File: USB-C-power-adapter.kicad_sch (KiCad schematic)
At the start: 65 parts, among them J1 USB-C_GCT_USB4105-GF-A, J2 JST_SH_1x4_SM04B-SRSS-TB-LF-SN, J3 Conn_Molex_NanoFit_1053131202, Q1 SQS401EN-T1_BE3, U1 TPD4E02B04DQA, U2 SIC477ED-T1-GE3, U3 STUSB4500_QFN, U4 TPD4E02B04DQA

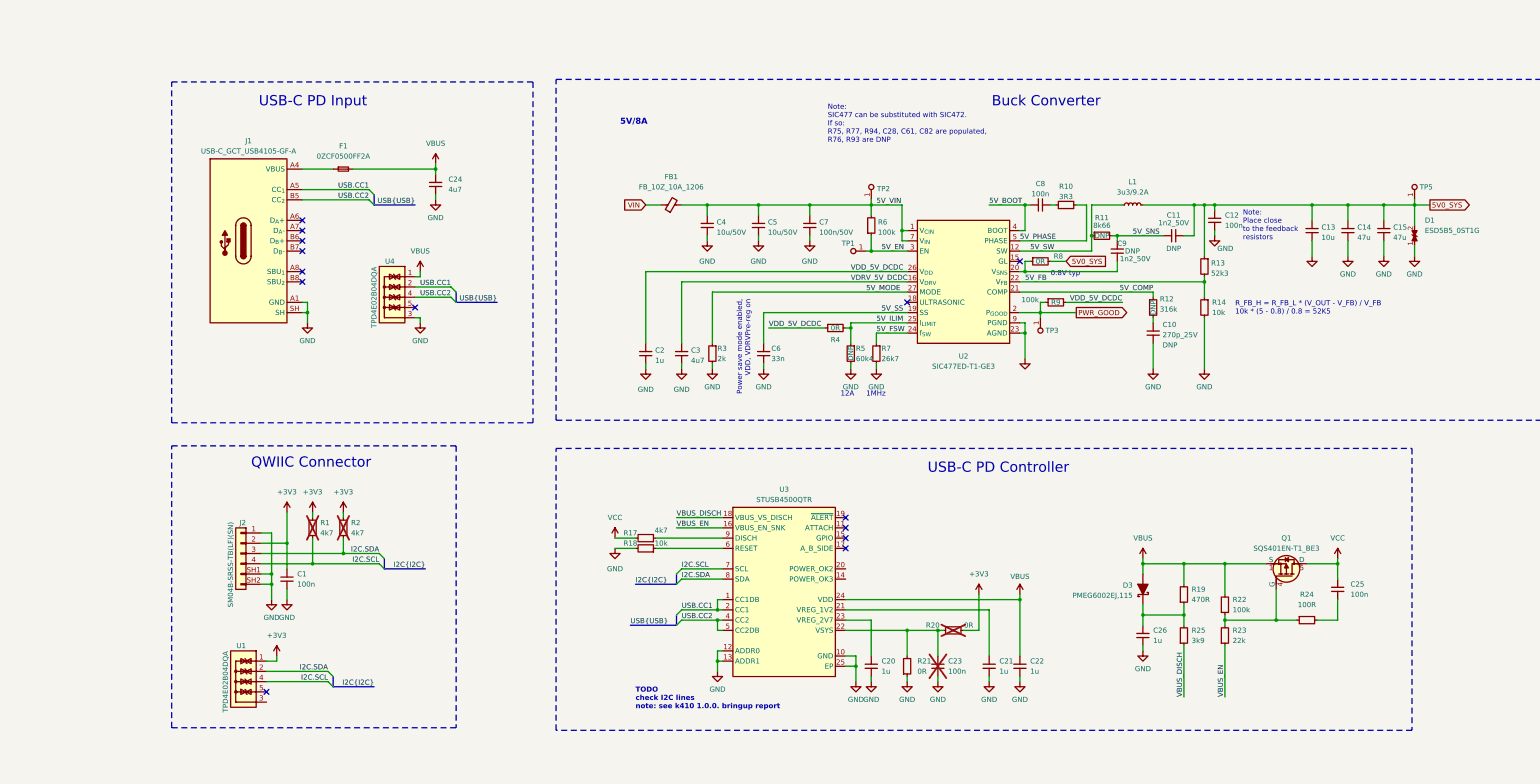
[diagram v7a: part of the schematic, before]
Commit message: [#57006] Change feedback resistors
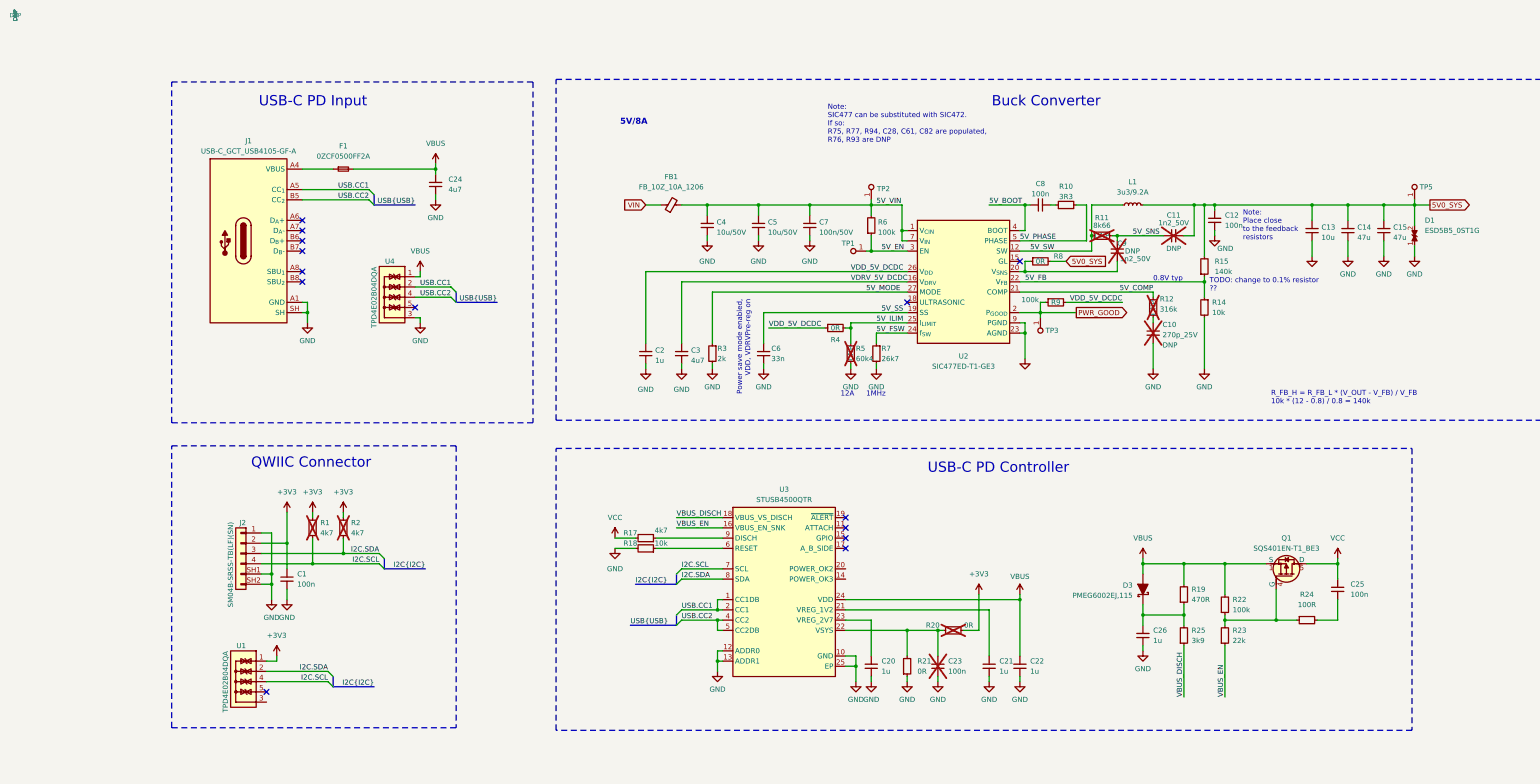
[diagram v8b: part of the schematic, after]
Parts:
- removed R13: R_52k3_0402, antmicro-footprints:R_0402_1005Metric, symbol antmicroResistors0402:R_52k3_0402
- added R15: R_140k_0402, antmicro-footprints:R_0402_1005Metric, symbol antmicroResistors0402:R_140k_0402
- C10, C11, C9, R11, R12, R5: now not fitted; now left out of the parts list
- C23, R1, R2, R20: DNP (none) -> DNP; now left out of the parts list
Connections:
- net 5V0_SYS: now also R15.2
- net 5V_FB: now also R15.1
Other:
- note added: "R_FB_H = R_FB_L * (V_OUT - V_FB) / V_FB 10k * (12 - 0.8) / 0.8 = 140k"
- note added: "TODO: change to 0.1% resistor ??"
- note removed: "R_FB_H = R_FB_L * (V_OUT - V_FB) / V_FB 10k * (5 - 0.8) / 0.8 = 52K5"
- note removed: "TODO check I2C lines note: see k410 1.0.0. bringup report"
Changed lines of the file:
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@@
     (effects (font (size 2.54 2.54)) (justify left bottom))
   )
-  (text "0.8V typ" (at 256.54 64.77 0)
+  (text "0.8V typ" (at 281.94 66.04 0)
     (effects (font (size 1.27 1.27)) (justify left bottom))
   )
@@
   (text "TODO\nadd the MOLEX nano fit 1053131202\nto the library "
     (at 91.44 217.805 0)
-    (effects (font (size 1.27 1.27)) (justify left bottom))
+    (effects (font (size 1.27 1.27) (color 255 0 0 1)) (justify left bottom))
   )
   (text "Note:\nSIC477 can be substituted with SIC472.\nIf so:\nR75, R77, R94, C28, C61, C82 are populated,\nR76, R93 are DNP"
@@
     (effects (font (size 1.27 1.27)) (justify left bottom))
   )
-  (text "TODO\ncheck I2C lines\nnote: see k410 1.0.0. bringup report\n"
-    (at 153.67 172.085 0)
-    (effects (font (size 1.27 1.27) (thickness 0.254) bold (color 255 0 0 1)) (justify left bottom))
-  )
   (text "1MHz" (at 210.82 94.615 0)
     (effects (font (size 1.27 1.27)) (justify left bottom))
@@
     (effects (font (size 2.54 2.54)) (justify left bottom))
   )
-  (text "R_FB_H = R_FB_L * (V_OUT - V_FB) / V_FB \n10k * (5 - 0.8) / 0.8 = 52K5"
-    (at 302.26 74.295 0)
+  (text "R_FB_H = R_FB_L * (V_OUT - V_FB) / V_FB \n10k * (12 - 0.8) / 0.8 = 140k\n"
+    (at 311.15 96.52 0)
     (effects (font (size 1.27 1.27)) (justify left bottom))
   )
+  (text "TODO: change to 0.1% resistor\n??\n" (at 295.91 68.58 0)
+    (effects (font (size 1.27 1.27) (color 255 0 0 1)) (justify left bottom))
+  )
   (label "5V_VIN" (at 213.36 46.99 0) (fields_autoplaced)
     (effects (font (size 1.27 1.27)) (justify left bottom))
@@
   )
   (symbol (lib_id "antmicroResistors0402:R_60k4_0402") (at 207.01 81.28 270) (unit 1)
-    (in_bom yes) (on_board yes) (dnp no)
+    (in_bom no) (on_board yes) (dnp yes)
     (property "Reference" "R5" (at 208.28 82.55 90)
       (effects (font (size 1.27 1.27)) (justify left))
@@
   )
   (symbol (lib_id "antmicroResistors0402:R_4k7_0402") (at 73.66 129.54 90) (unit 1)
-    (in_bom yes) (on_board yes) (dnp yes) (fields_autoplaced)
+    (in_bom no) (on_board yes) (dnp yes) (fields_autoplaced)
     (property "Reference" "R1" (at 75.565 125.73 90)
       (effects (font (size 1.27 1.27) (thickness 0.15)) (justify right))
@@
       (effects (font (size 1.27 1.27)) (justify left bottom) hide)
     )
+    (property "DNP" "DNP" (at 0 0 0)
+      (effects (font (size 1 1)))
+    )
     (pin "2")
     (pin "1")
@@
   )
   (symbol (lib_id "antmicroCapacitors0402:C_1n2_50V_0402") (at 273.05 60.96 90) (unit 1)
-    (in_bom yes) (on_board yes) (dnp no)
+    (in_bom no) (on_board yes) (dnp yes)
     (property "Reference" "C9" (at 273.05 56.515 90)
       (effects (font (size 1.27 1.27)) (justify right))
@@
   )
   (symbol (lib_id "antmicroResistors0402:R_0R_0402") (at 229.87 152.4 0) (unit 1)
-    (in_bom yes) (on_board yes) (dnp yes)
+    (in_bom no) (on_board yes) (dnp yes)
     (property "Reference" "R20" (at 227.33 151.13 0)
       (effects (font (size 1.27 1.27) (thickness 0.15)))
@@
       (effects (font (size 1.27 1.27) (thickness 0.15)) (justify left bottom) hide)
     )
+    (property "DNP" "DNP" (at 0 0 0)
+      (effects (font (size 1 1)))
+    )
     (pin "1")
     (pin "2")
@@
   )
   (symbol (lib_id "antmicroCapacitors0402:C_1n2_50V_0402") (at 284.48 54.61 0) (unit 1)
-    (in_bom yes) (on_board yes) (dnp no)
+    (in_bom no) (on_board yes) (dnp yes)
     (property "Reference" "C11" (at 287.02 49.53 0)
       (effects (font (size 1.27 1.27)))
@@
     )
   )
+  (symbol (lib_id "antmicroResistors0402:R_140k_0402") (at 294.64 64.77 90) (unit 1)
+    (in_bom yes) (on_board yes) (dnp no) (fields_autoplaced)
+    (property "Reference" "R15" (at 297.18 60.96 90)
+      (effects (font (size 1.27 1.27) (thickness 0.15)) (justify right))
+    )
+    (property "Value" "R_140k_0402" (at 307.34 44.45 0)
+      (effects (font (size 1.27 1.27) (thickness 0.15)) (justify left bottom) hide)
+    )
+    (property "Footprint" "antmicro-footprints:R_0402_1005Metric" (at 309.88 44.45 0)
+      (effects (font (size 1.27 1.27) (thickness 0.15)) (justify left bottom) hide)
+    )
+    (property "Datasheet" "https://www.bourns.com/docs/product-datasheets/cr.pdf" (at 312.42 44.45 0)
+      (effects (font (size 1.27 1.27) (thickness 0.15)) (justify left bottom) hide)
+    )
+    (property "MPN" "CR0402-FX-1403GLF" (at 314.96 44.45 0)
+      (effects (font (size 1.27 1.27) (thickness 0.15)) (justify left bottom) hide)
+    )
+    (property "Manufacturer" "Bourns" (at 317.5 44.45 0)
+      (effects (font (size 1.27 1.27) (thickness 0.15)) (justify left bottom) hide)
+    )
+    (property "License" "Apache-2.0" (at 320.04 44.45 0)
+      (effects (font (size 1.27 1.27) (thickness 0.15)) (justify left bottom) hide)
+    )
+    (property "Author" "Antmicro" (at 322.58 44.45 0)
+      (effects (font (size 1.27 1.27) (thickness 0.15)) (justify left bottom) hide)
+    )
+    (property "Val" "140k" (at 297.18 63.5 90)
+      (effects (font (size 1.27 1.27) (thickness 0.15)) (justify right))
+    )
+    (property "Tolerance" "1%" (at 304.8 44.45 0)
+      (effects (font (size 1.27 1.27)) (justify left bottom) hide)
+    )
+    (pin "2")
+    (pin "1")
+    (instances
+      (project "USB-C-power-adapter"
+        (path "/8da33aa8-79ed-467a-95ed-bf58aa0d1db6"
+          (reference "R15") (unit 1)
+        )
+      )
+    )
+  )
   (symbol (lib_id "antmicropower:GND") (at 207.01 87.63 0) (unit 1)
     (in_bom yes) (on_board yes) (dnp no) (fields_autoplaced)
@@
   )
   (symbol (lib_id "antmicroResistors0402:R_4k7_0402") (at 81.28 129.54 90) (unit 1)
-    (in_bom yes) (on_board yes) (dnp yes) (fields_autoplaced)
+    (in_bom no) (on_board yes) (dnp yes) (fields_autoplaced)
     (property "Reference" "R2" (at 83.185 125.73 90)
       (effects (font (size 1.27 1.27) (thickness 0.15)) (justify right))
@@
       (effects (font (size 1.27 1.27)) (justify left bottom) hide)
     )
+    (property "DNP" "DNP" (at 0 0 0)
+      (effects (font (size 1 1)))
+    )
     (pin "2")
     (pin "1")
@@
     )
   )
-  (symbol (lib_id "antmicroResistors0402:R_52k3_0402") (at 294.64 59.69 270) (unit 1)
-    (in_bom yes) (on_board yes) (dnp no) (fields_autoplaced)
-    (property "Reference" "R13" (at 296.291 61.3953 90)
-      (effects (font (size 1.27 1.27)) (justify left))
-    )
-    (property "Value" "R_52k3_0402" (at 290.83 59.69 0)
-      (effects (font (size 1.27 1.27)) (justify left) hide)
-    )
-    (property "Footprint" "antmicro-footprints:R_0402_1005Metric" (at 299.72 64.77 0)
-      (effects (font (size 1.27 1.27)) (justify left) hide)
-    )
-    (property "Datasheet" "https://www.bourns.com/docs/product-datasheets/cr.pdf" (at 294.64 59.69 0)
-      (effects (font (size 1.27 1.27)) (justify left) hide)
-    )
-    (property "Manufacturer" "Bourns" (at 304.8 64.77 0)
-      (effects (font (size 1.27 1.27)) (justify left) hide)
-    )
-    (property "MPN" "CR0402-FX-5232GLF" (at 302.26 64.77 0)
-      (effects (font (size 1.27 1.27)) (justify left) hide)
-    )
-    (property "Val" "52k3" (at 296.291 63.9322 90)
-      (effects (font (size 1.27 1.27)) (justify left))
-    )
-    (property "License" "Apache-2.0" (at 269.24 80.01 0)
-      (effects (font (size 1.27 1.27) (thickness 0.15)) (justify left) hide)
-    )
-    (property "Author" "Antmicro" (at 266.7 80.01 0)
-      (effects (font (size 1.27 1.27) (thickness 0.15)) (justify left) hide)
-    )
-    (property "Tolerance" "1%" (at 284.48 80.01 0)
-      (effects (font (size 1.27 1.27)) (justify left) hide)
-    )
-    (pin "1")
-    (pin "2")
-    (instances
-      (project "USB-C-power-adapter"
-        (path "/8da33aa8-79ed-467a-95ed-bf58aa0d1db6"
-          (reference "R13") (unit 1)
-        )
-      )
-    )
-  )
   (symbol (lib_id "antmicropower:GND") (at 171.45 55.88 0) (unit 1)
     (in_bom yes) (on_board yes) (dnp no) (fields_autoplaced)
@@
   )
   (symbol (lib_id "antmicroResistors0402:R_316k_0402") (at 281.94 69.85 90) (mirror x) (unit 1)
-    (in_bom yes) (on_board yes) (dnp no) (fields_autoplaced)
+    (in_bom no) (on_board yes) (dnp yes) (fields_autoplaced)
     (property "Reference" "R12" (at 283.591 70.2869 90)
       (effects (font (size 1.27 1.27)) (justify right))
@@
   )
   (symbol (lib_id "antmicroCapacitors0402:C_100n_0402") (at 228.6 163.83 90) (unit 1)
-    (in_bom yes) (on_board yes) (dnp yes) (fields_autoplaced)
+    (in_bom no) (on_board yes) (dnp yes) (fields_autoplaced)
     (property "Reference" "C23" (at 231.14 160.0136 90)
       (effects (font (size 1.27 1.27) (thickness 0.15)) (justify right))
@@
       (effects (font (size 1.27 1.27)) (justify left bottom) hide)
     )
+    (property "DNP" "DNP" (at 0 0 0)
+      (effects (font (size 1 1)))
+    )
     (pin "2")
     (pin "1")
@@
   )
   (symbol (lib_id "antmicroCapacitors0402:C_270p_25V_0402") (at 281.94 76.2 90) (mirror x) (unit 1)
-    (in_bom yes) (on_board yes) (dnp no) (fields_autoplaced)
+    (in_bom no) (on_board yes) (dnp yes) (fields_autoplaced)
     (property "Reference" "C10" (at 284.2641 76.6432 90)
       (effects (font (size 1.27 1.27)) (justify right))
@@
   )
   (symbol (lib_id "antmicroResistors0402:R_8k66_0402") (at 266.7 54.61 0) (unit 1)
-    (in_bom yes) (on_board yes) (dnp no)
+    (in_bom no) (on_board yes) (dnp yes)
     (property "Reference" "R11" (at 269.24 50.165 0)
       (effects (font (size 1.27 1.27)))
